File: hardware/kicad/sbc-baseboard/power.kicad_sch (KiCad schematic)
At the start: 86 parts, among them J17 Qwiic PD, J2 USB-C PD in, Q101 2N7002, Q102 2N7002, U101 STUSB4500QTR, U102 PCA9517A, U103 TPS54560BDDA, U104 TPS54560BDDA, U105 TPS62823DLC

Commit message: USB 2.0 differential pairs named for the router; USB net class; ports aligned
Every USB 2.0 data net is now <base>_P / <base>_N, the suffixes KiCad's PCB
editor pairs up: J1_D, J3_D, PORT1_D..PORT4_D on the receptacle side of each
ESD array; HUB_UP and HUB_DN1..HUB_DN7 at the hub; K64_USB and FTDI_USB at the
chips. All 15 pairs are complete with D+ on _P. The project file gains a USB
net class assigned by pattern (differential geometry to be set from the
stackup). The labels sit at wire ends with their text along the pair's own
wire; routes now run their last leg into a side pin as one wire so a label at
the pin end owns the stretch (Conn join=False keeps a shared stub where two
routes meet at one pin). The USB-A receptacles and their switches move down
1.27 mm so the pairs run straight from the ESD arrays, and the port ESD arrays
move left to make room for the labels. Netlist membership unchanged (356
nets); ERC, geometry, connectivity, layout and reproducibility gates all
clean.

Co-Authored-By: Claude Fable 5.1 <noreply@anthropic.com>
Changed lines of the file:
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@@
 		(pts
 			(xy 66.04 72.39)
-			(xy 109.22 72.39)
-		)
-		(stroke
-			(width 0)
-			(type default)
-		)
-	)
-	(wire
-		(pts
-			(xy 109.22 72.39)
 			(xy 132.08 72.39)
 		)
@@
 		(pts
 			(xy 67.31 80.01)
-			(xy 109.22 80.01)
-		)
-		(stroke
-			(width 0)
-			(type default)
-		)
-	)
-	(wire
-		(pts
-			(xy 109.22 80.01)
 			(xy 132.08 80.01)
 		)

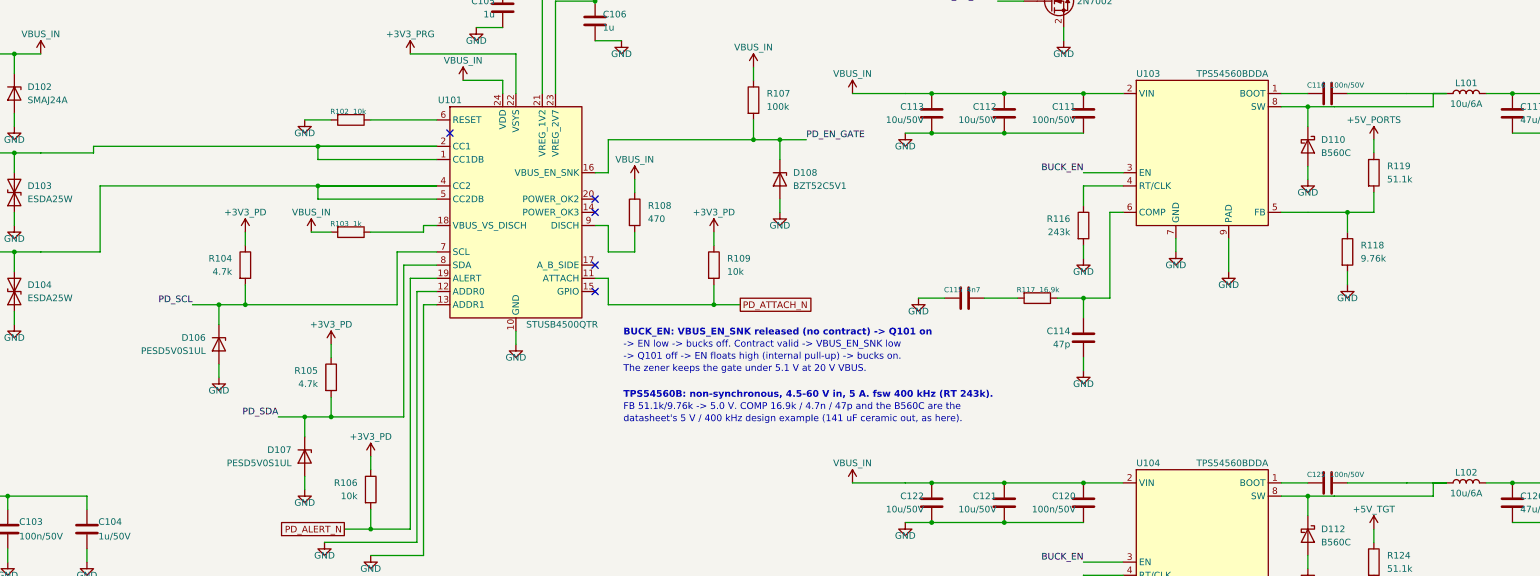
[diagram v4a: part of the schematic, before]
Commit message: Nothing drawn over anything else; FTDI Friend header; DAPLink per FRDM-K64F; 90 ohm USB class
Geometry gate now also reports two wires sharing a stretch, and is at zero on
every sheet. Routes into a stacked connector from one side take staggered
columns and rows; the signal relays are flipped so COM meets the header's
first pin without crossings; the opto-isolator moves above the passthrough
wires and taps the relay's COM lane; a tag before a route ends at the route's
target; routes into joined pins end at the join; the K64's VREGIN diode taps
the VBUS lane beside the ESD's stub; symbol mirrors are applied after
rotation, as KiCad does.

FT231X: the 3V3OUT lane stays on its pin row with its capacitor far out, clear
of the VCC decoupling; J9 mirrors the Adafruit FTDI Friend (VCC 5 V and pin 6
RTS by default on bridged solder jumpers; the first pass had left J9's VCC on
an open jumper only).

DAPLink K20, verified against DAPLink k20dx and the FRDM-K64F OpenSDA circuit:
PTC7 (SWDIO_IN) joins the SWDIO net, 33 R series resistors on the K20's USB
pair (K20_USB_P/N), notes and spec questions 12 and 14 resolved.

USB net class: 0.35 mm / 0.20 mm for 90 ohm on Advanced Circuits' standard
4-layer 62 mil stackup (spec section 8a). ERC 0, geometry 0, merges 0, layout
0, builds reproducible.

Co-Authored-By: Claude Fable 5.1 <noreply@anthropic.com>
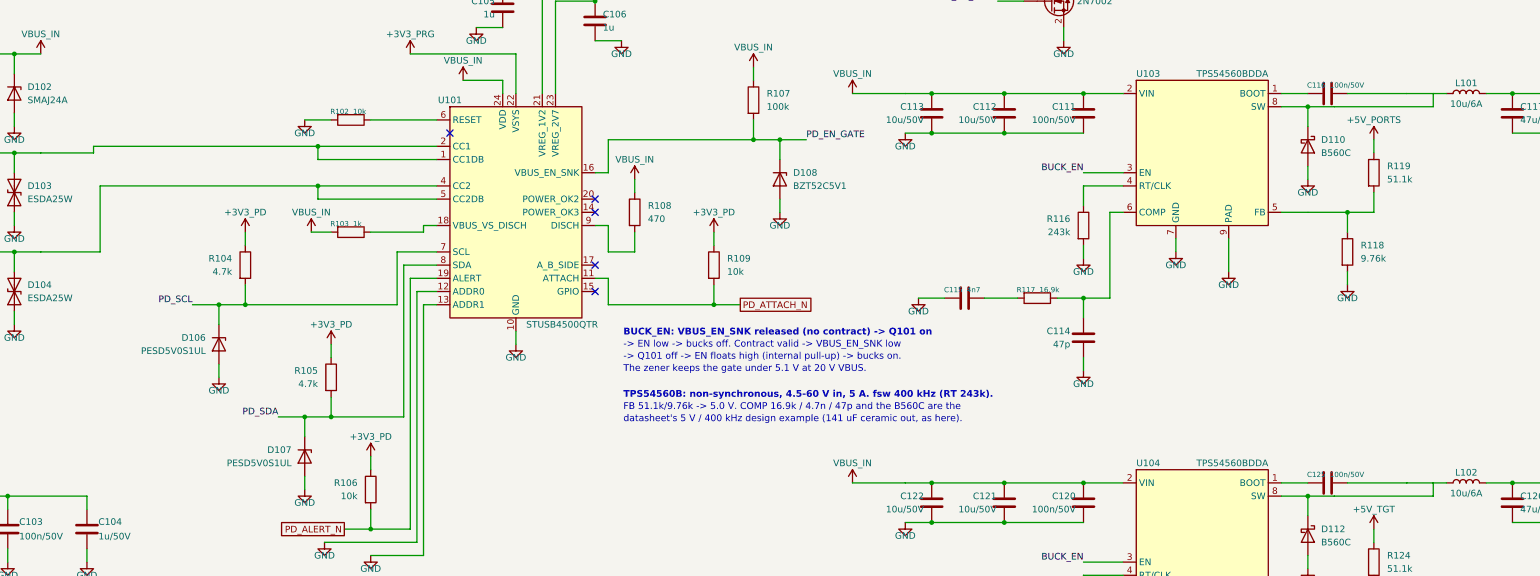
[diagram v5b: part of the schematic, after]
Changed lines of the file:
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@@
 		(pts
 			(xy 66.04 72.39)
-			(xy 132.08 72.39)
+			(xy 109.22 72.39)
 		)
 		(stroke
@@
 		(pts
 			(xy 67.31 80.01)
-			(xy 132.08 80.01)
+			(xy 109.22 80.01)
 		)
 		(stroke
@@
 	(wire
 		(pts
-			(xy 323.85 62.23)
-			(xy 326.39 62.23)
-		)
-		(stroke
-			(width 0)
-			(type default)
-		)
-	)
-	(wire
-		(pts
 			(xy 294.64 85.09)
 			(xy 299.72 85.09)
@@
 		)
 		(stroke
-			(width 0)
-			(type default)
-		)
-	)
-	(wire
-		(pts
-			(xy 323.85 137.16)
-			(xy 326.39 137.16)
-		)
-		(stroke

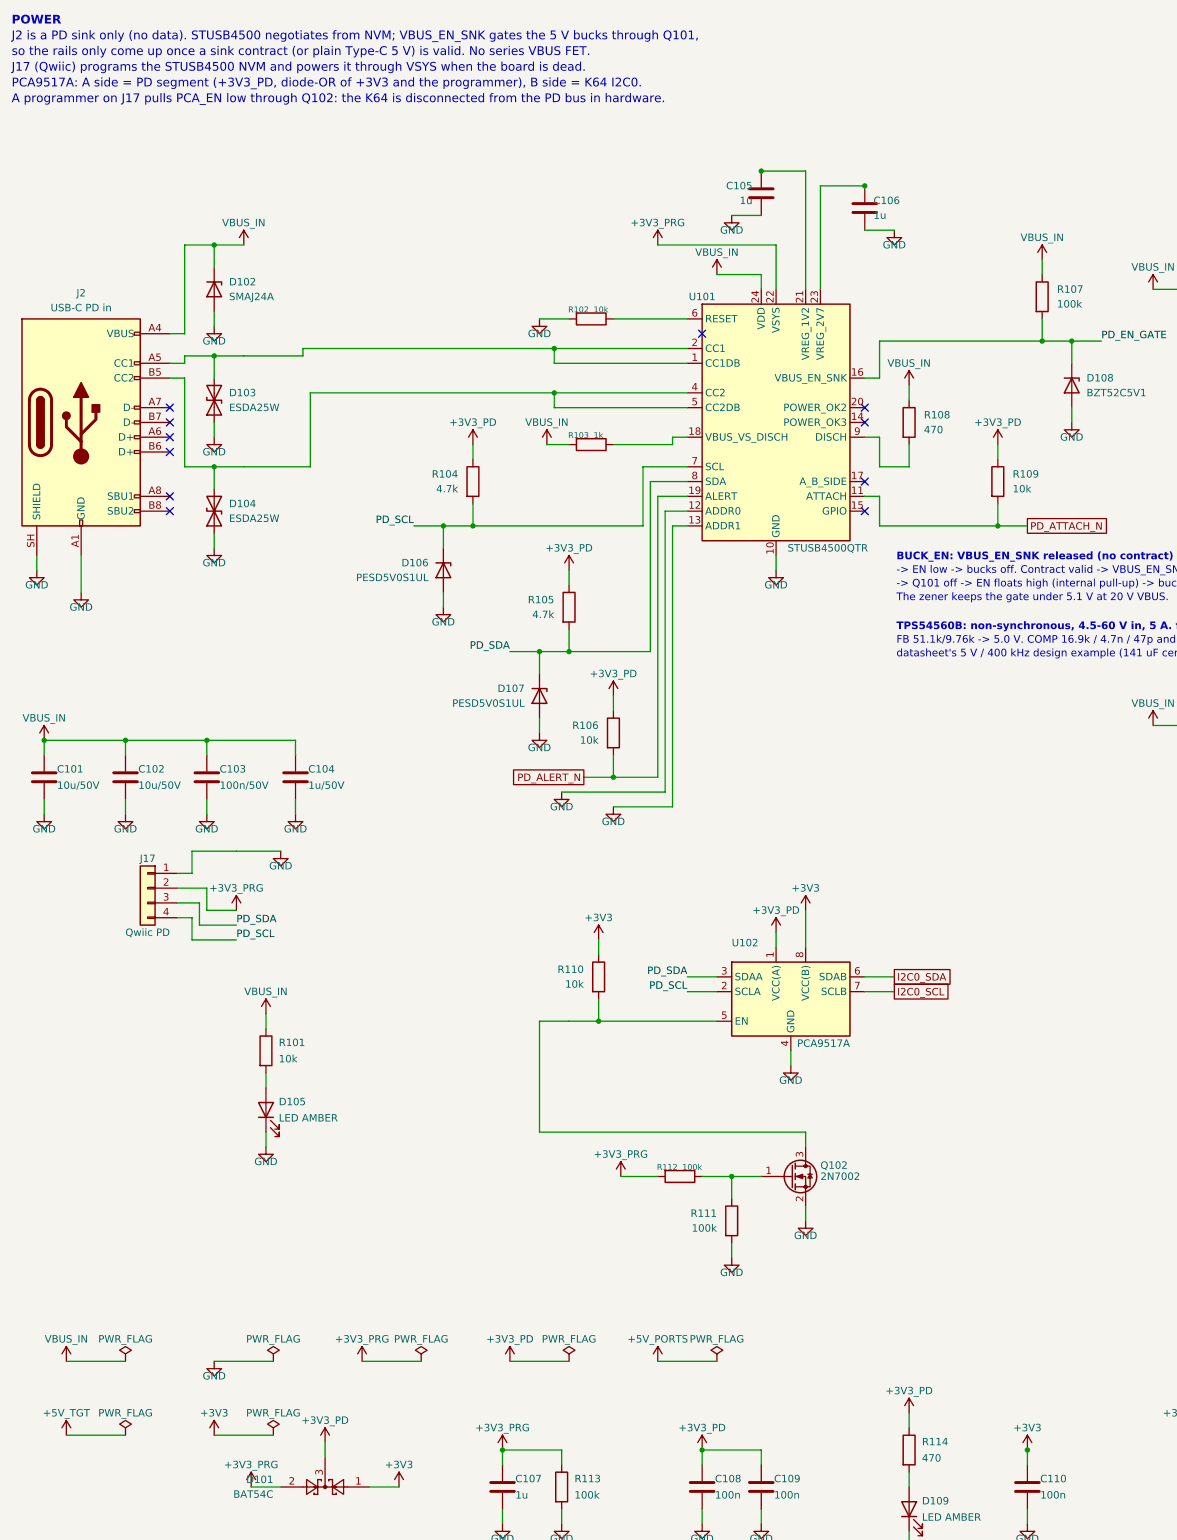
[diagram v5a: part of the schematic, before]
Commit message: Current pathways annotated on the sheets; net classes PSU_3A, USB_VBUS_3A, PWR_6A; layout directives
Net class directive flags on every high-current net, with the class name
carrying the current: the PSU passthrough (PSU_VP, PSU_VOUT, PSU_GND, now
named), the USB port and FTDI VBUS, VBUS_IN, and the +5V_PORTS / +5V_TGT rails
on the power sheet's flag strip. The project file carries the classes with
their widths and patterns; the XML netlist confirms every net's class. Sheet
notes state the currents and widths. Spec: FTDI header section rewritten for
the Adafruit FTDI Friend defaults (a deliberate exception to the back-feed
rule), current-pathway table in 8a. docs/layout-directives.md written from
the spec for the layout generator.

Co-Authored-By: Claude Fable 5.1 <noreply@anthropic.com>
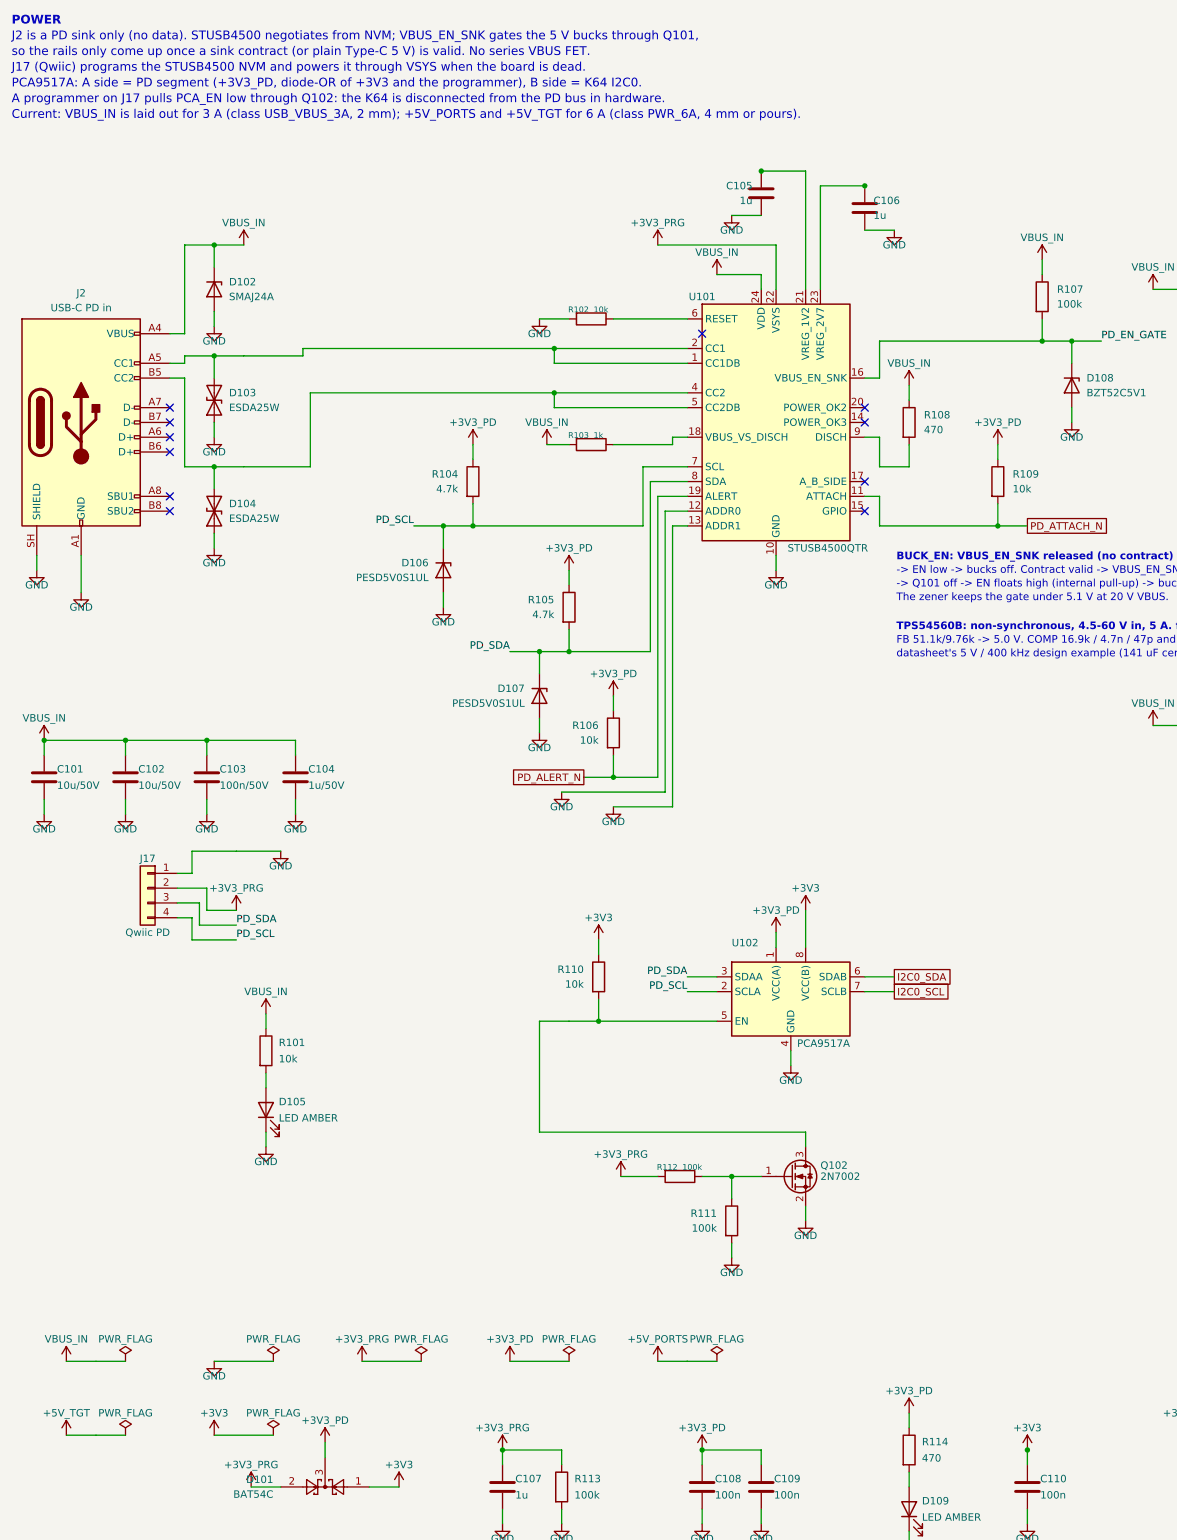
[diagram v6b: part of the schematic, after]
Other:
- note added: "Current: VBUS_IN is laid out for 3 A (class USB_VBUS_3A, 2 mm); +5V_PORTS and +5V_TGT for 6 A (class PWR_6A, 4 mm or pours)."
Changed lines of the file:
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@@
 		)
 	)
+	(text "Current: VBUS_IN is laid out for 3 A (class USB_VBUS_3A, 2 mm); +5V_PORTS and +5V_TGT for 6 A (class PWR_6A, 4 mm or pours)."
+		(exclude_from_sim no)
+		(at 16 33.2 0)
+		(effects
+			(font
+				(size 1.5 1.5)
+			)
+			(justify left bottom)
+		)
+	)
 	(symbol
 		(lib_id "Connector:USB_C_Receptacle_USB2.0_16P")
@@
 		(pts
 			(xy 25.4 246.38)
+			(xy 30.48 246.38)
+		)
+		(stroke
+			(width 0)
+			(type default)
+		)
+	)
+	(wire
+		(pts
+			(xy 30.48 246.38)
 			(xy 35.56 246.38)
 		)
@@
 		)
 	)
+	(netclass_flag ""
+		(length 2.54)
+		(shape round)
+		(at 30.48 246.38 270)
+		(fields_autoplaced no)
+		(effects
+			(font
+				(size 1.27 1.27)
+			)
+			(justify left bottom)
+		)
+		(property "Netclass" "USB_VBUS_3A"
+			(at 31.48 250.12 0)
+			(effects
+				(font
+					(size 1.27 1.27)
+					(italic yes)
+				)
+				(justify left)
+			)
+		)
+	)
 	(symbol
 		(lib_id "power:GND")
@@
 		(pts
 			(xy 127 246.38)
+			(xy 132.08 246.38)
+		)
+		(stroke
+			(width 0)
+			(type default)
+		)
+	)
+	(wire
+		(pts
+			(xy 132.08 246.38)
 			(xy 137.16 246.38)
 		)
@@
 		)
 	)
+	(netclass_flag ""
+		(length 2.54)
+		(shape round)
+		(at 132.08 246.38 270)
+		(fields_autoplaced no)
+		(effects
+			(font
+				(size 1.27 1.27)
+			)
+			(justify left bottom)
+		)
+		(property "Netclass" "PWR_6A"
+			(at 133.08 250.12 0)
+			(effects
+				(font
+					(size 1.27 1.27)
+					(italic yes)
+				)
+				(justify left)
+			)
+		)
+	)
 	(symbol
 		(lib_id "power:+5V")
@@
 		(pts
 			(xy 25.4 259.08)
+			(xy 30.48 259.08)
+		)
+		(stroke
+			(width 0)
+			(type default)
+		)
+	)
+	(wire
+		(pts
+			(xy 30.48 259.08)
 			(xy 35.56 259.08)
 		)
@@
 		)
 	)
+	(netclass_flag ""
+		(length 2.54)
+		(shape round)
+		(at 30.48 259.08 270)
+		(fields_autoplaced no)
+		(effects
+			(font
+				(size 1.27 1.27)
+			)
+			(justify left bottom)
+		)
+		(property "Netclass" "PWR_6A"
+			(at 31.48 262.82 0)
+			(effects
+				(font
+					(size 1.27 1.27)
+					(italic yes)
+				)
+				(justify left)
+			)
+		)
+	)

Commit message: First board: generated placement from the layout directives; current classes on the sheets
gen/pcb.py (pcbnew) builds sbc-baseboard.kicad_pcb once from the netlist, the
project file and gen/layout.py (docs/layout-directives.md as data): 140 x 80
outline with 2 mm corners, M3 holes on GND with corner keep-outs, the Advanced
Circuits 4-layer stackup, every footprint with its nets, edge connectors facing
outward (USB-C on their footprint's PCB Edge mark), interior parts packed by
function next to their connectors, the L2 ground plane with an isolated PSU_GND
island, and sbc-baseboard.kicad_dru with the passthrough's keep-out and 2 mm
creepage rules. DRC: no errors but twelve inside the GCT USB-C footprints
(hole to shield pad 0.19 mm against the fab's 0.25), 499 unrouted; silk left
for layout. The project file now carries the fab's constraints and the classes
PSU_3A, USB_VBUS_3A, PWR_6A, PSU_ISO; net class directive flags mark every
high-current net on the sheets; the opto's sense nets are named.

Directives revised at layout: J17 top-entry inboard (the RJ45 measures 22 mm),
J19 beside J18 (one compact isolated region), J9 on the right edge.

Co-Authored-By: Claude Fable 5.1 <noreply@anthropic.com>
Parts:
- J17: footprint Connector_JST:JST_SH_SM04B-SRSS-TB_1x04-1MP_P1.00mm_Horizontal -> Connector_JST:JST_SH_BM04B-SRSS-TB_1x04-1MP_P1.00mm_Vertical
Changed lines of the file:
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@@
 			)
 		)
-		(property "Footprint" "Connector_JST:JST_SH_SM04B-SRSS-TB_1x04-1MP_P1.00mm_Horizontal"
+		(property "Footprint" "Connector_JST:JST_SH_BM04B-SRSS-TB_1x04-1MP_P1.00mm_Vertical"
 			(at 39.37 165.1 0)
 			(hide yes)

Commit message: The three USB-C receptacles use the house GCT footprint with the peg holes clear of the outer ground pads: DRC at zero errors
gen/kit.py points USBC at calico:USB_C_Receptacle_GCT_USB4105-xx-A_16P_TopMnt_Horizontal_PegClear
(ecad-libraries 0.3.5, submodule bumped): KiCad's footprint rebuilt pad for pad
with A1, A12, B1 and B12 0.1 mm shorter at the peg end, hole to copper 0.29 mm
against the fab's 0.25 mm. Schematic rebuilt (ERC clean, the footprint field on
J1-J3, BOM, PDF), board regenerated with the placement unchanged; the twelve
hole-clearance errors are gone. README and the reference-design review record
the deviation from GCT's drawing.

Co-Authored-By: Claude Fable 5.1 <noreply@anthropic.com>
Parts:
- J2: footprint Connector_USB:USB_C_Receptacle_GCT_USB4105-xx-A_16P_TopMnt_Horizontal -> calico:USB_C_Receptacle_GCT_USB4105-xx-A_16P_TopMnt_Horizontal_PegClear
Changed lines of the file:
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@@
 			)
 		)
-		(property "Footprint" "Connector_USB:USB_C_Receptacle_GCT_USB4105-xx-A_16P_TopMnt_Horizontal"
+		(property "Footprint" "calico:USB_C_Receptacle_GCT_USB4105-xx-A_16P_TopMnt_Horizontal_PegClear"
 			(at 27.94 85.09 0)
 			(hide yes)
